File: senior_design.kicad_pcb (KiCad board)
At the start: 2 copper layers, 128.6 x 80.8 mm, 114 parts, among them J1 Conn_ARM_JTAG_SWD_20, J2 Conn_01x03_Pin, J3 Conn_01x09_Socket, J4 USB_B_Micro, J5 Out_to_display, J6 AudioJack3, J7 SD_Card_Receptacle, SW1 SW_SPST, U1 Boost Converter - TPS61169DCKR, U10 WE-TVS-824015043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

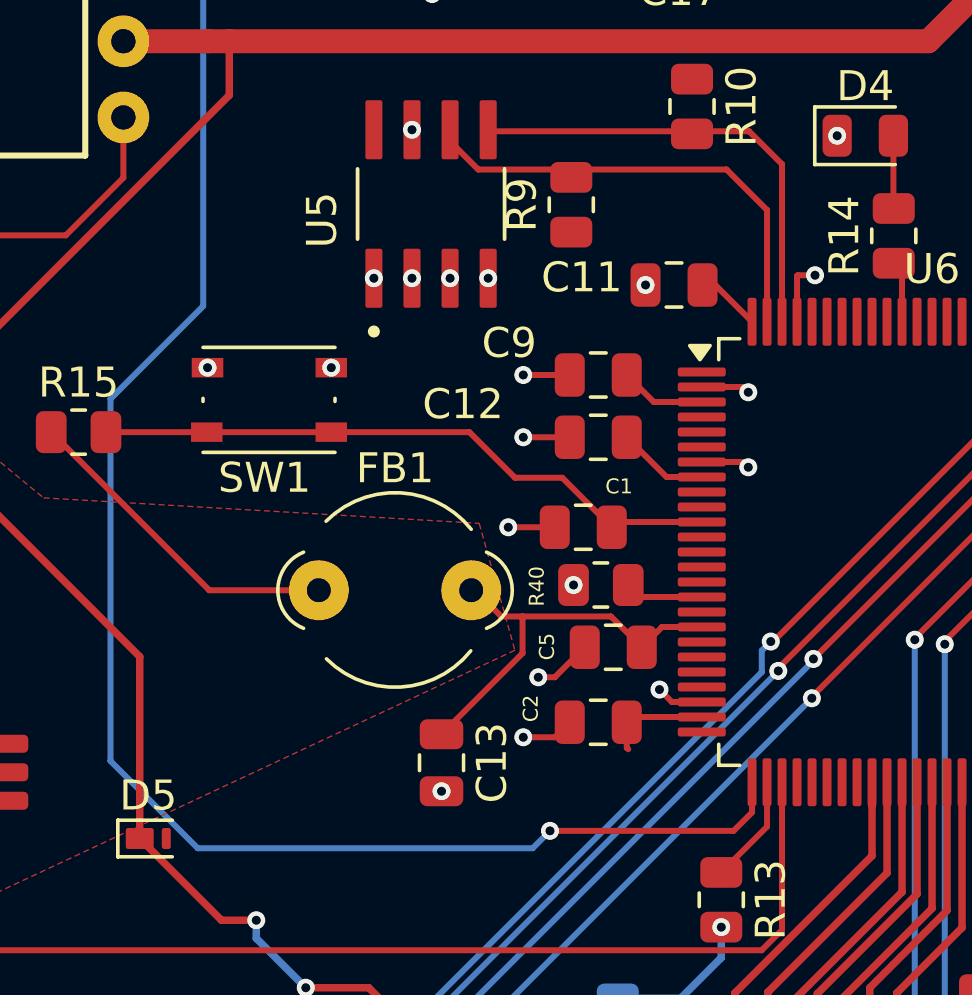
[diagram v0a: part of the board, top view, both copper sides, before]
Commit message: added HSE
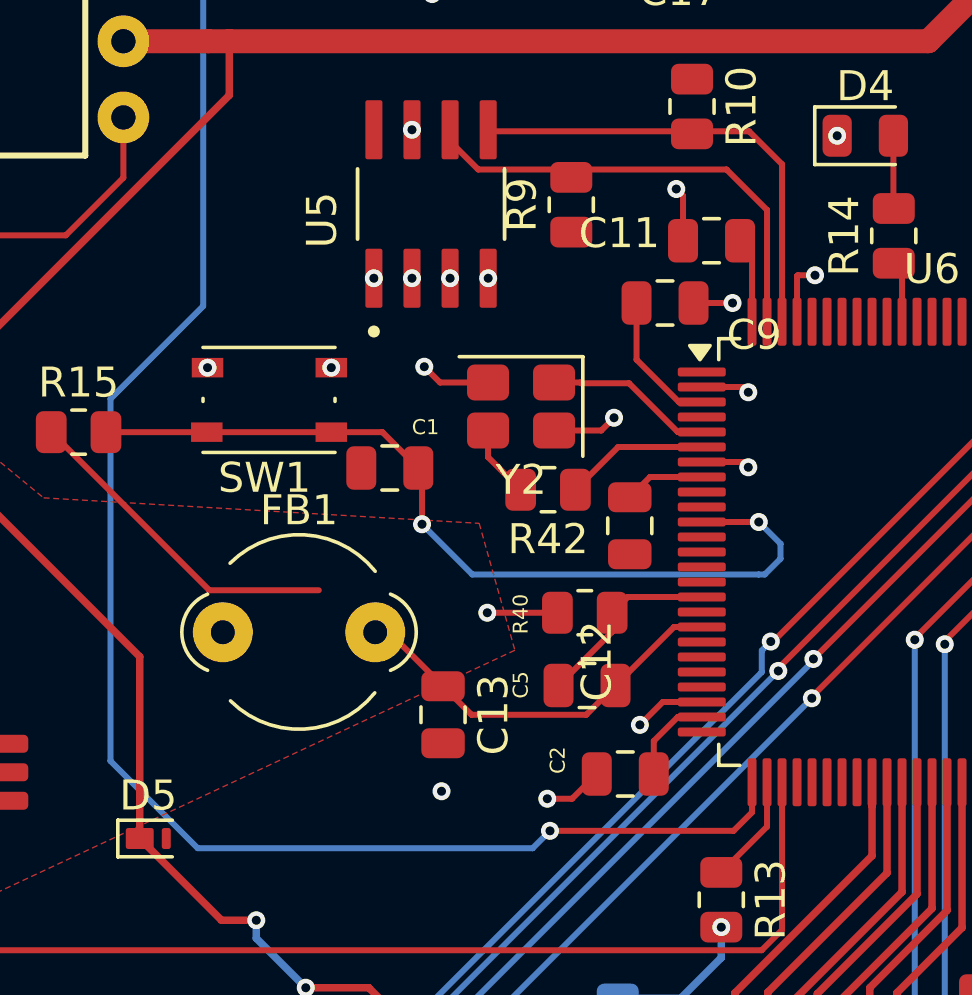
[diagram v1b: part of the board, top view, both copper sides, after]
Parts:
- added R42: 1K, Resistor_SMD:R_0805_2012Metric, F.Cu at (180.8, 82.2)
- added Y2: 8MHz, Crystal:Crystal_SMD_SeikoEpson_FA238-4Pin_3.2x2.5mm, F.Cu at (179.9, 79.5)
- moved C1 6.75 mm to (175.6, 81.5)
- moved FB1 3.49 mm to (170.0, 87.0)
- moved C9 3.27 mm to (184.7, 76.0), turned to 0 degrees
- moved C12 3.13 mm to (183.6, 83.5), turned to -90 degrees
- moved C2 1.95 mm to (183.4, 91.7)
- moved C11 1.93 mm to (186.3, 74.0)
- moved C13 1.60 mm to (177.3, 89.8)
- moved C5 1.55 mm to (182.1, 88.8)
- moved R40 1.07 mm to (182.1, 86.3)
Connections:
- U6 pad 5: unconnected-(U6-PC14-Pad5) -> /MCU/OSC_IN
- U6 pad 6: unconnected-(U6-PC15-Pad6) -> /MCU/OSC_OUT
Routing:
- net /MCU/SWD_RESET: track 21.2 -> 29.2 mm, vias 0 -> 2
- net GND: track 112.2 -> 119.7 mm, vias 53 -> 52
- net /MCU/OSC_IN: track 0.00 -> 5.61 mm
- net /MCU/OSC_OUT: track 0.00 -> 4.80 mm
- net Net-(R42-Pad2): track 0.00 -> 2.43 mm
- net GNDA: track 34.3 -> 36.1 mm
- net +3.3V: track 117.2 -> 118.9 mm
- net VDDA: track 21.6 -> 21.0 mm

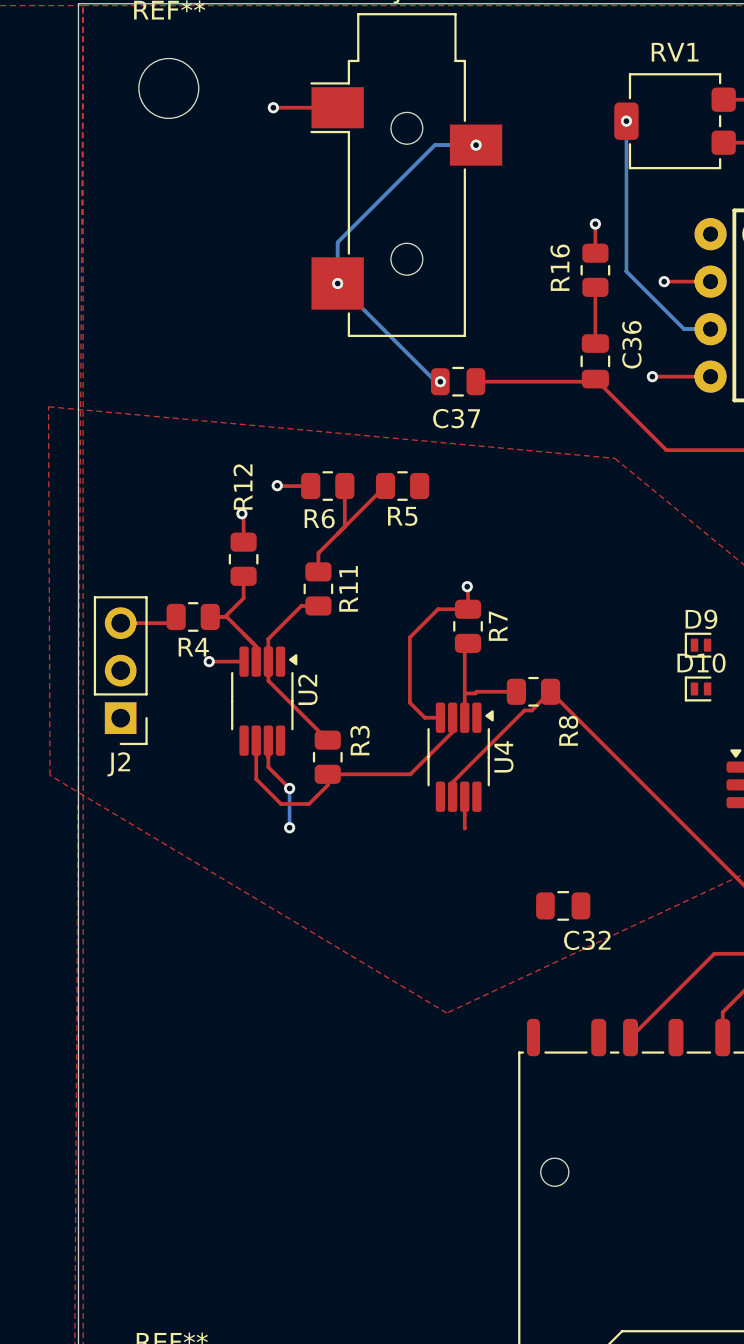
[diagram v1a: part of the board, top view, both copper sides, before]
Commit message: Updated Audio with ESD Diode
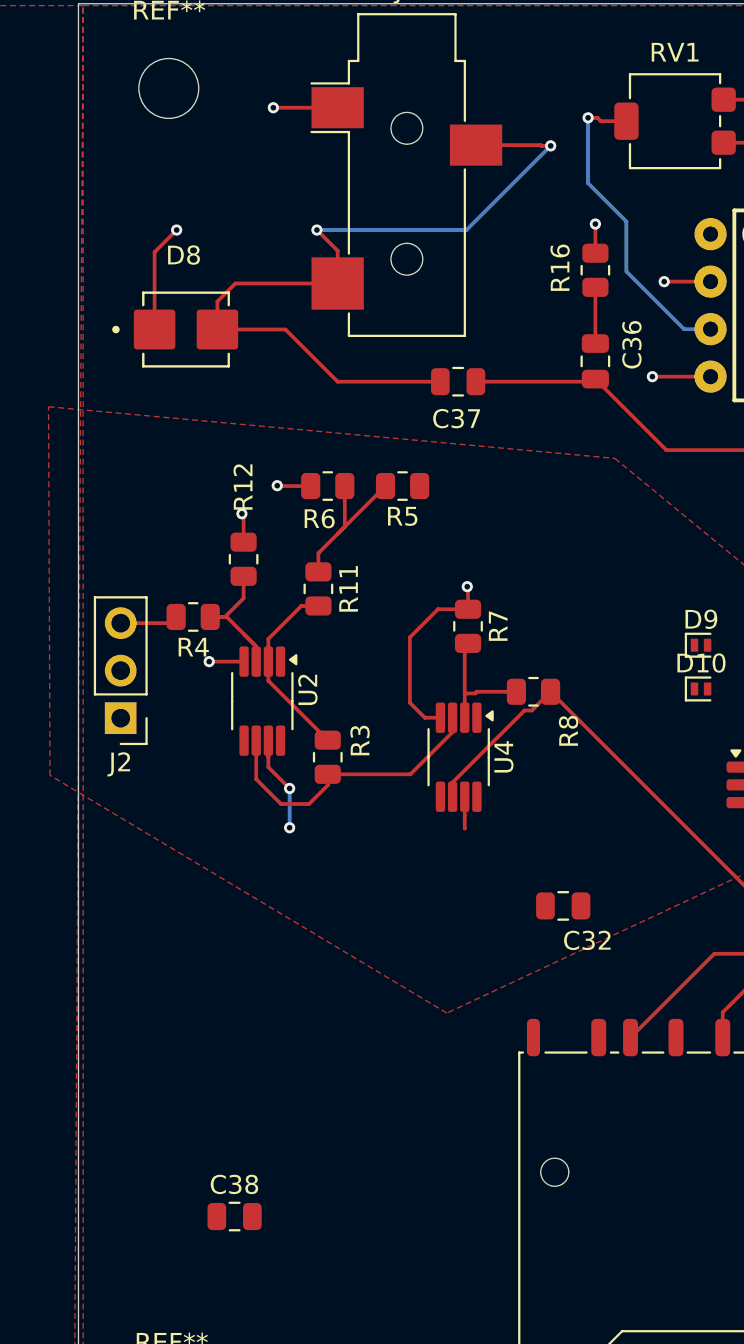
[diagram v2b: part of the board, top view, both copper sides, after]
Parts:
- added C38: 100nF, Capacitor_SMD:C_0805_2012Metric, F.Cu at (133.6, 114.8)
- added D8: D_TVS, Audio_Module:D_TVS SMB, F.Cu at (131.0, 67.3)
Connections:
- net AUDIO_IN renamed DAC_OUT1
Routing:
- net Net-(D8-A2): track 19.4 -> 43.3 mm, vias 3 -> 2
- net GNDA: track 36.1 -> 41.9 mm, vias 7 -> 8
- net Net-(U8-+): track 13.8 -> 17.0 mm

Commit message: added HE2 and expanded VDDA plane
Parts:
- added D11: PESD3V3S1UL, Diode_SMD:D_SOD-882, F.Cu at (127.6, 90.9)
- added D12: PESD3V3S1UL, Diode_SMD:D_SOD-882, F.Cu at (130.4, 97.5)
- added J8: Conn_01x03_Pin, Connector_PinHeader_2.54mm:PinHeader_1x03_P2.54mm_Vertical, F.Cu at (127.4, 104.9)
- added R43: 22k, Resistor_SMD:R_0805_2012Metric, F.Cu at (141.8, 95.8)
- added R44: 22k, Resistor_SMD:R_0805_2012Metric, F.Cu at (139.0, 95.0)
- added R45: 1.9k, Resistor_SMD:R_0805_2012Metric, F.Cu at (137.5, 99.6)
- added R46: 1.9k, Resistor_SMD:R_0805_2012Metric, F.Cu at (131.4, 99.8)
- added R47: 1.9k, Resistor_SMD:R_0805_2012Metric, F.Cu at (134.9, 96.4)
- added R48: 1.9k, Resistor_SMD:R_0805_2012Metric, F.Cu at (139.0, 105.9)
- added R49: 1k, Resistor_SMD:R_0805_2012Metric, F.Cu at (145.6, 97.1)
- added R50: 3.6k, Resistor_SMD:R_0805_2012Metric, F.Cu at (151.5, 101.0)
- added U12: OPA196xDGK, Package_SO:VSSOP-8_3x3mm_P0.65mm, F.Cu at (135.4, 105.0)
- added U13: OPA196xDGK, Package_SO:VSSOP-8_3x3mm_P0.65mm, F.Cu at (145.2, 103.1)
- D3: moved to F.Cu
- moved D10 37.7 mm to (127.3, 107.5), turned to -90 degrees
- moved D9 28.5 mm to (130.2, 80.6), turned to 90 degrees
- moved C38 27.8 mm to (156.2, 98.7)
- moved D3 5.15 mm to (181.9, 95.1), turned to 0 degrees
- moved R13 1.32 mm to (185.6, 95.1), turned to 180 degrees
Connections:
- net DAC_OUT1 renamed AUDIO_IN
- U6 pad 30: unconnected-(U6-PB1-Pad30) -> ADC_IN2
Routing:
- net ADC_IN2: track 0.00 -> 52.1 mm
- net Net-(U13-+): track 0.00 -> 17.6 mm
- net Net-(U13--): track 0.00 -> 9.10 mm
- net Net-(U12--): track 0.00 -> 8.16 mm
- net Net-(U12-+): track 0.00 -> 8.04 mm
- net Net-(D12-K): track 0.00 -> 5.06 mm
- net VDDA: track 21.0 -> 25.9 mm
- net Net-(R43-Pad2): track 0.00 -> 3.33 mm
- net Net-(D3-A): track 5.03 -> 1.83 mm, vias 1 -> 0
- net Net-(D9-K): track 3.10 -> 4.90 mm
- net ADC_IN1: track 55.9 -> 54.7 mm
- net /MCU/LED1: track 3.64 -> 4.14 mm
- added copper zone on B.Cu, net GND
- removed copper zone on F.Cu, net GND

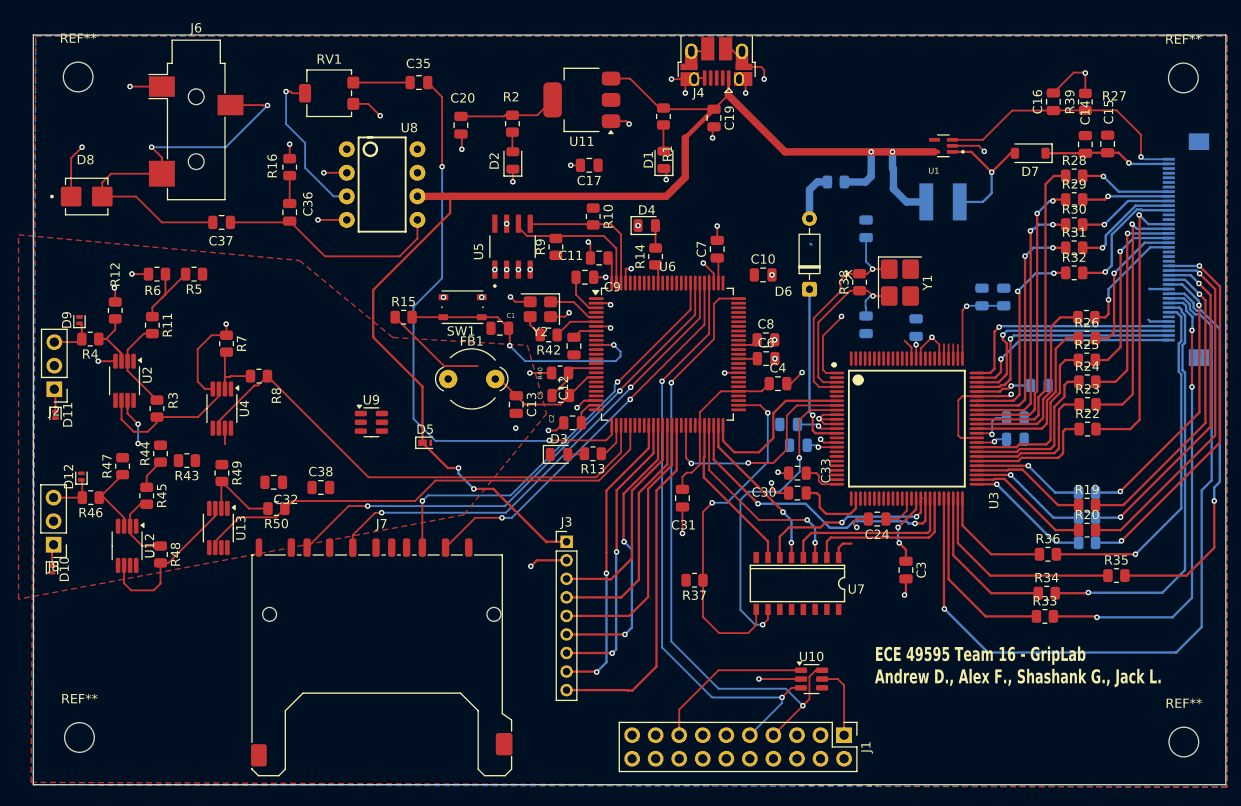
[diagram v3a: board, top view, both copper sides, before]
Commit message: fixed a bunch of DRC errors
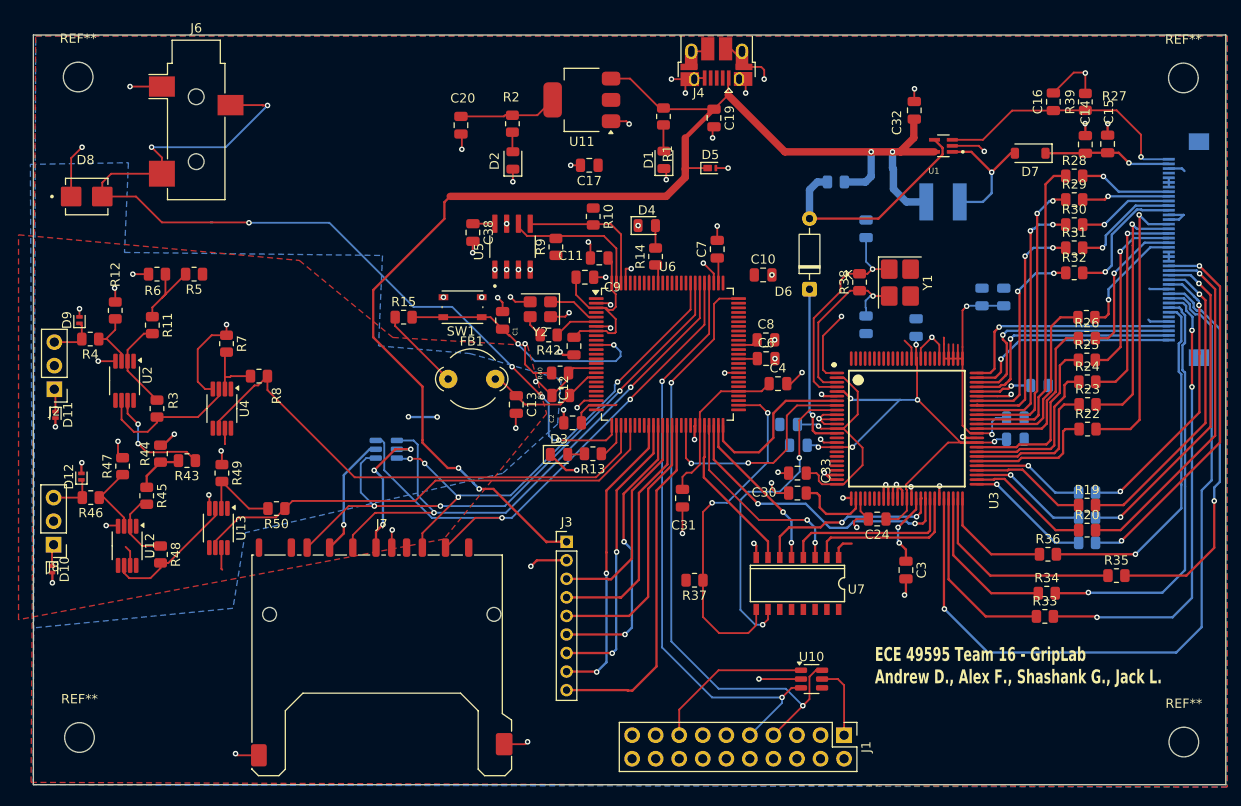
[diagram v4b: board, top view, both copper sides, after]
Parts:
- removed C35: 10 uF, Capacitor_SMD:C_0805_2012Metric
- removed C36: 0.1 uF, Capacitor_SMD:C_0805_2012Metric
- removed C37: 250 uF, Capacitor_SMD:C_0805_2012Metric
- removed R16: 10 Ω, Resistor_SMD:R_0805_2012Metric
- removed RV1: R_Potentiometer_US, Potentiometer_SMD:Potentiometer_Bourns_3214G_Horizontal
- removed U8: LM386, Library:LM386
- U9: moved to B.Cu
- moved C32 79.9 mm to (220.2, 58.0), turned to 90 degrees
- moved D5 42.7 mm to (198.2, 64.2)
- moved C38 32.0 mm to (172.7, 71.2), turned to -90 degrees
- moved U9 3.32 mm to (163.3, 94.6)
- moved C1 0.90 mm to (175.8, 80.7), turned to -90 degrees
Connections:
- D8 pad 1: GNDA -> GND
- D8 pad 2: Net-(D8-A2) -> DAC_OUT1
- J6 pad R: Net-(D8-A2) -> DAC_OUT1
- J6 pad S: GNDA -> GND
- J6 pad T: Net-(D8-A2) -> DAC_OUT1
- U6 pad 26: AUDIO_IN -> DAC_OUT1
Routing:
- net DAC_OUT1: track 0.00 -> 99.2 mm, vias 0 -> 6
- net GND: track 119.7 -> 187.2 mm, vias 52 -> 73
- net AUDIO_IN: track 61.9 -> 0.00 mm, vias 2 -> 0
- net Net-(D8-A2): track 43.3 -> 0.00 mm, vias 2 -> 0
- net +3.3V: track 118.9 -> 161.2 mm
- net +1V5: track 13.0 -> 55.2 mm, vias 3 -> 6
- net Net-(C36-Pad2): track 24.6 -> 0.00 mm
- net Net-(D6-A): track 5.39 -> 24.6 mm
- net SPI_SSD: track 42.5 -> 61.3 mm
- net Net-(U8-+): track 17.0 -> 0.00 mm, vias 1 -> 0
- net +3V3: track 0.00 -> 15.6 mm, vias 0 -> 3
- net VDDA: track 25.9 -> 40.6 mm, vias 2 -> 4
- net SPI_SCLK: track 52.3 -> 62.8 mm
- net SPI_MISO: track 55.7 -> 62.8 mm, vias 2 -> 3
- net SPI_MOSI: track 45.8 -> 52.3 mm, vias 2 -> 4
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- added copper zone on B.Cu, net GNDA

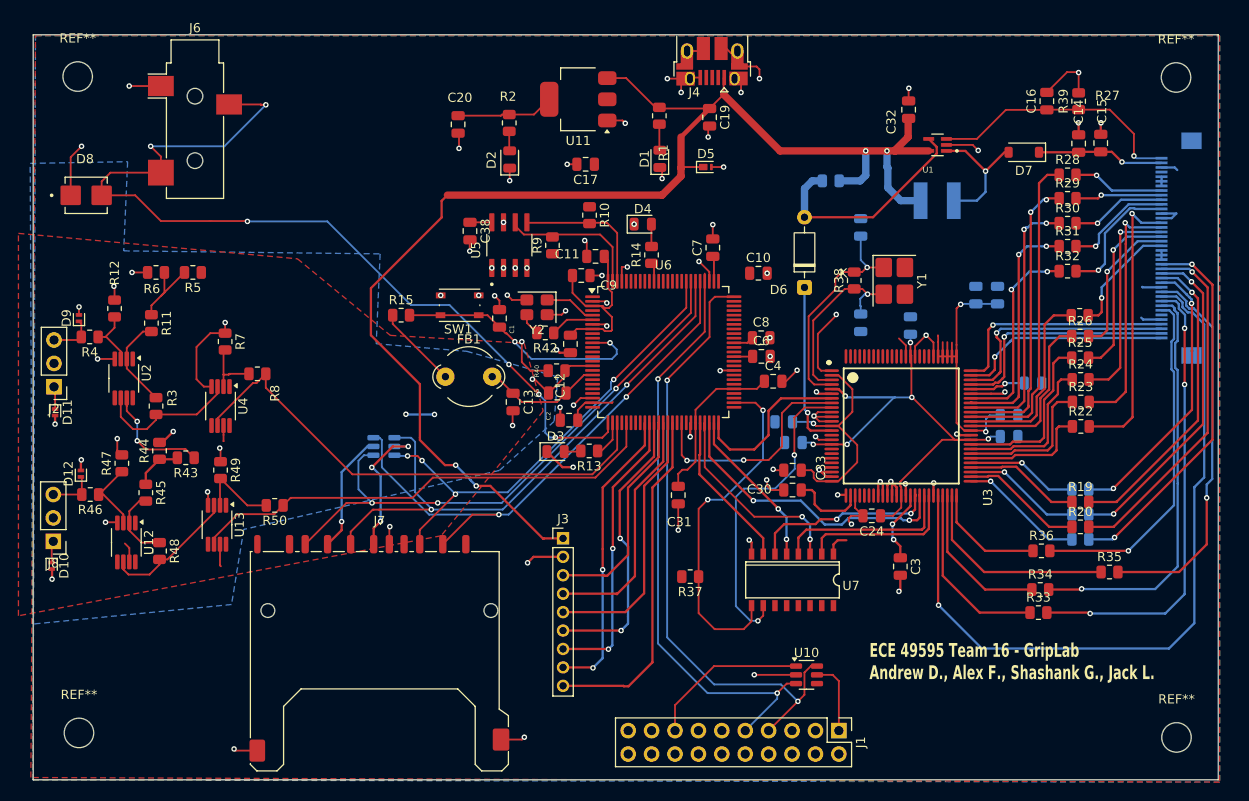
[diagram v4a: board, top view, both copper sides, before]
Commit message: added 10 pin stlink and fixed a bunch of errors and warnings
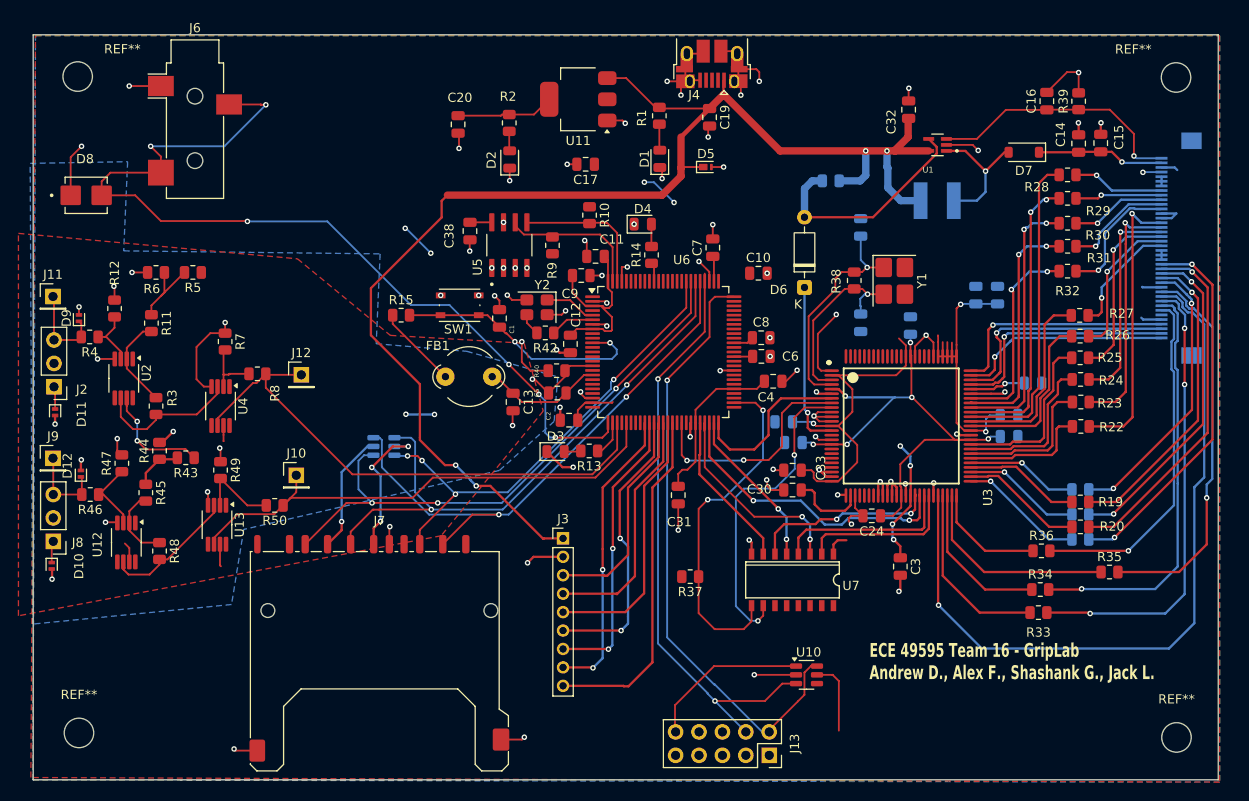
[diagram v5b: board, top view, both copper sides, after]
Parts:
- removed J1: Conn_ARM_JTAG_SWD_20, Connector_PinHeader_2.54mm:PinHeader_2x10_P2.54mm_Vertical
- added J10: Conn_01x01_Pin, Connector_PinHeader_2.54mm:PinHeader_1x01_P2.54mm_Vertical, F.Cu at (153.8, 97.7)
- added J11: Conn_01x01_Pin, Connector_PinHeader_2.54mm:PinHeader_1x01_P2.54mm_Vertical, F.Cu at (127.4, 78.3)
- added J12: Conn_01x01_Pin, Connector_PinHeader_2.54mm:PinHeader_1x01_P2.54mm_Vertical, F.Cu at (154.3, 86.8)
- added J13: Conn_ARM_JTAG_SWD_10, Connector_PinSocket_2.54mm:PinSocket_2x05_P2.54mm_Vertical, F.Cu at (205.1, 128.1)
- added J9: Conn_01x01_Pin, Connector_PinHeader_2.54mm:PinHeader_1x01_P2.54mm_Vertical, F.Cu at (127.4, 95.8)
- moved J4 0.29 mm to (198.9, 53.1)
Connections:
- net DAC_OUT1 renamed AUDIO_IN
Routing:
- net +3.3V: track 161.2 -> 186.7 mm, vias 5 -> 12
- net Net-(D9-K): track 4.90 -> 9.66 mm
- net Net-(D12-K): track 5.06 -> 9.01 mm
- net ADC_IN1: track 55.6 -> 59.5 mm
- net ADC_IN2: track 52.1 -> 56.0 mm
- net GND: track 187.2 -> 189.6 mm
- net /MCU/SWDIO: track 67.9 -> 66.2 mm, vias 2 -> 1
- net +1V5: track 55.2 -> 56.3 mm
